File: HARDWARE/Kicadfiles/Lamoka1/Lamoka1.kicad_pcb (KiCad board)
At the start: 2 copper layers, 95 x 95 mm, 124 parts, among them IC1 INA240A2DR, J1 2606-1108/010-000, J2 2606-1352, J3 USB_C_Receptacle_USB2.0_14P, J4 470531000, J5 2604-1103, Q1 25V 60A N-Ch, Q2 30V 56A N-Ch, Q3 100V 150A N-Ch, Q4 100V 150A N-Ch, Q5 100V 150A N-Ch, Q6 100V 150A N-Ch, SW1 B3F-4055, U1 RP2354A, U10 ADS7128IRTER, U2 AMS1117-3.3, U3 74AHCT1G125, U4 LM5122MH/NOPB, U5 UCC27735DR, U6 UCC27735DR, U7 TPS62160DSGR, U8 TMP235A2DBZR, U9 TMP235A2DBZR, X1 ABM8-272-T3

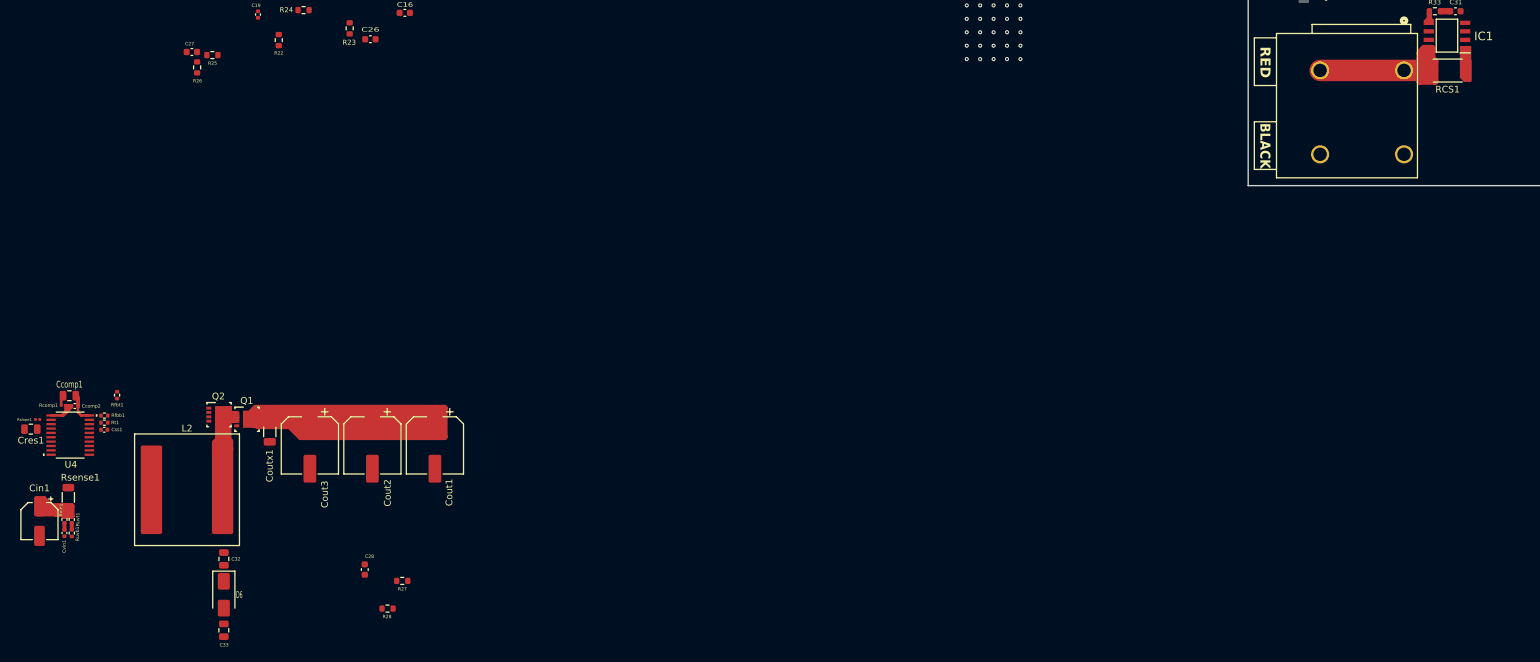
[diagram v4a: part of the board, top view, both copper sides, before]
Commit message: general routing for the Lamoka1/2
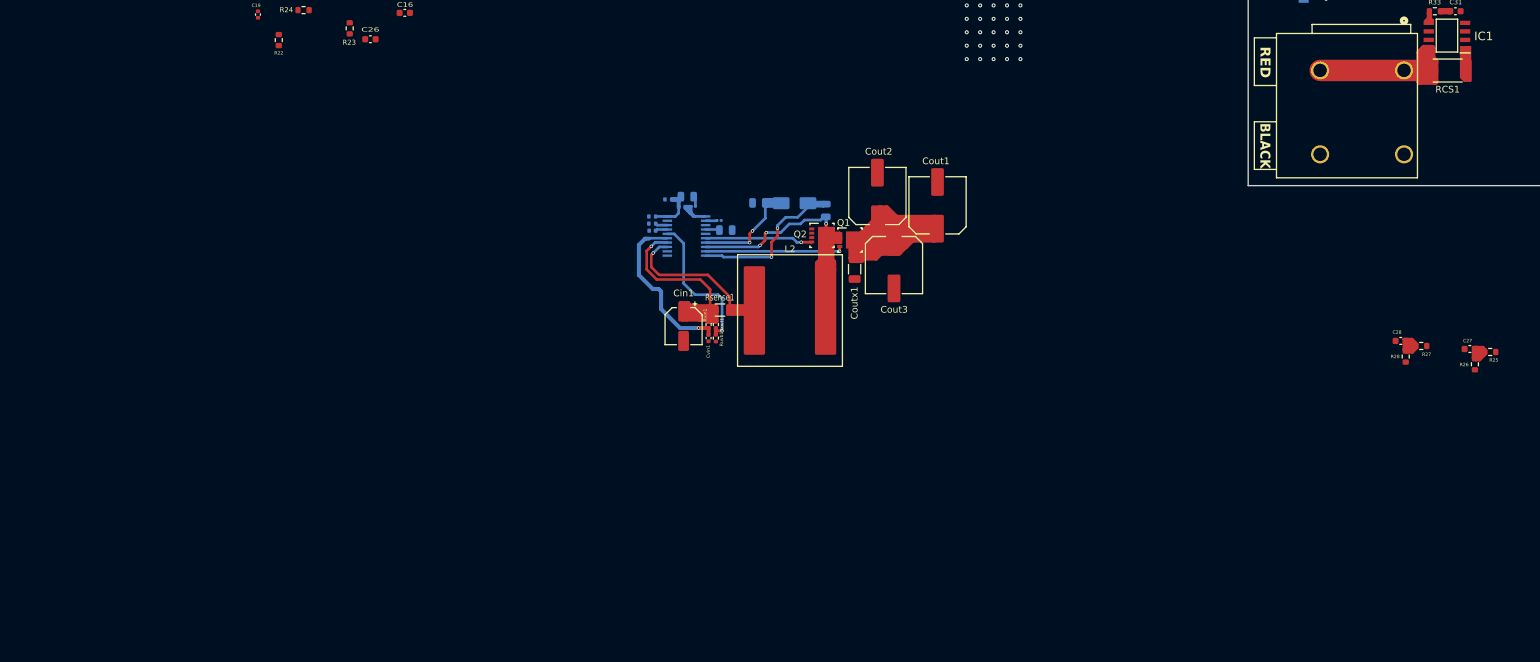
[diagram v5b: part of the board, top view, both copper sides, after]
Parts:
- C32, C33, Ccomp1, Ccomp2, Cres1, Css1, D6, Rcomp1, Rfbb1, Rfbt1, Rslope1, Rt1, U4: moved to B.Cu
- moved C27 195.4 mm to (365.1, 299.9)
- moved R25 195.4 mm to (368.2, 300.4)
- moved R26 195.4 mm to (365.9, 302.2)
- moved C28 158.0 mm to (354.9, 298.7), turned to 180 degrees
- moved R28 156.2 mm to (355.6, 301.1), turned to -90 degrees
- moved R27 155.8 mm to (357.9, 299.5)
- moved Cres1 107.7 mm to (254.3, 282.2), turned to 0 degrees
- moved Rslope1 105.8 mm to (253.3, 280.8), turned to 0 degrees
- moved C32 103.6 mm to (269.2, 279.3), turned to -90 degrees
- moved D6 103.1 mm to (264.6, 278.2), turned to 180 degrees
- moved C33 102.0 mm to (259.2, 278.2), turned to 0 degrees
- moved Rsense1 101.0 mm to (253.4, 294.1), turned to 0 degrees
- moved Cvin1 100.2 mm to (251.7, 298.3)
- moved Ruvb1 100.2 mm to (252.8, 298.3)
- moved Cin1 100.2 mm to (248.0, 296.5)
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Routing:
- net /Inversion-Section/G4D: track 238.8 -> 174.5 mm
- net /Inversion-Section/CSN: track 0.00 -> 54.0 mm, vias 0 -> 1
- net /Inversion-Section/BST: track 0.00 -> 35.6 mm, vias 0 -> 2
- net /Inversion-Section/CSP: track 157.9 -> 182.6 mm, vias 0 -> 1
- net /Inversion-Section/VCC: track 0.00 -> 24.5 mm, vias 0 -> 2
- net /Inversion-Section/VIN: track 1.02 -> 25.3 mm, vias 0 -> 1
- net /Inversion-Section/SW: track 56.8 -> 79.9 mm, vias 0 -> 3
- net /Inversion-Section/UVLO: track 1.00 -> 22.4 mm, vias 0 -> 1
- net /Inversion-Section/HO: track 0.00 -> 20.7 mm, vias 0 -> 1
- net /Control-Section/AIN0: track 0.00 -> 19.0 mm
- net /Control-Section/AIN1: track 0.00 -> 17.6 mm
- net /Inversion-Section/LO: track 0.00 -> 16.1 mm, vias 0 -> 1
- net /Inversion-Section/FB: track 4.48 -> 10.3 mm
- net /Inversion-Section/RES: track 0.00 -> 2.09 mm
- net /Inversion-Section/SYNCIN_RT: track 0.00 -> 1.83 mm
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
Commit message: more routing
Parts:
- removed H3, H4, H5, H6, H7, H8: MountingHole, MountingHole:MountingHole_3.2mm_M3
- C12, C13, U2: moved to F.Cu
- C16, C17, C18, C26, R22, R23, R24, R4, R7: moved to B.Cu
- moved H2 233.6 mm to (417.0, 270.4)
- moved C18 186.2 mm to (365.6, 225.4), turned to -100 degrees
- moved R24 183.2 mm to (374.4, 240.6), turned to 180 degrees
- moved C19 177.1 mm to (359.3, 221.1), turned to -90 degrees
- moved R23 176.4 mm to (374.4, 242.2), turned to 180 degrees
- moved R7 165.0 mm to (360.8, 216.2), turned to -90 degrees
- moved C26 163.2 mm to (364.1, 241.4), turned to 180 degrees
- moved C17 159.9 mm to (364.6, 225.2), turned to -100 degrees
- moved C15 159.4 mm to (360.5, 226.0), turned to 0 degrees
- moved C14 157.6 mm to (360.6, 222.2), turned to -90 degrees
- moved C16 156.8 mm to (361.2, 224.2), turned to 170 degrees
- moved R4 155.1 mm to (363.3, 225.4), turned to -100 degrees
- moved R22 154.9 mm to (341.3, 234.2), turned to 90 degrees
- moved Cout1 136.6 mm to (421.2, 259.9), turned to -90 degrees
- moved Cout2 136.4 mm to (412.2, 259.9), turned to -90 degrees
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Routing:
- net /Inversion-Section/CSP: track 182.6 -> 328.0 mm, vias 1 -> 2
- net /Buck-5v: track 49.9 -> 70.6 mm
- net /Control-Section/USB-5v: track 7.22 -> 23.3 mm
- net /Inversion-Section/G4D: track 174.5 -> 190.2 mm
- net /Control-Section/1V1: track 0.00 -> 12.9 mm, vias 0 -> 1
- net /Control-Section/BTN: track 0.00 -> 12.5 mm
- net /Control-Section/VREG_GND: track 0.00 -> 12.1 mm, vias 0 -> 1
- net /Inversion-Section/VIN: track 25.3 -> 19.4 mm
- net /Control-Section/3v3: track 0.00 -> 5.83 mm, vias 0 -> 1
- net Net-(U1-VREG_LX): track 0.00 -> 5.79 mm
- net /GPIO5: track 0.03 -> 4.71 mm
- net Net-(U1-VREG_AVDD): track 0.00 -> 4.53 mm
- net /Inversion-Section/CSN: track 54.0 -> 54.6 mm

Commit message: MORE ROUTING FOR THE LAMOKA1/2, JUST CONTROL RELATED STUFF HERE
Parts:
- U8: moved to B.Cu
- moved G*** 106.1 mm to (379.3, 218.7)
- moved NT1 67.3 mm to (360.9, 227.8), turned to -135 degrees
- moved C12 55.3 mm to (342.2, 211.9)
- moved C13 55.3 mm to (339.9, 207.2)
- moved U2 55.3 mm to (345.3, 207.2)
- moved U8 44.1 mm to (369.9, 227.5), turned to 0 degrees
- moved C26 29.7 mm to (380.5, 216.7)
- moved R23 29.7 mm to (390.7, 217.5)
- moved R24 29.7 mm to (390.7, 215.9)
- moved U10 29.7 mm to (384.2, 217.8)
- moved U9 22.7 mm to (409.7, 209.2)
- moved R5 3.94 mm to (350.1, 219.1)
- moved R6 3.94 mm to (350.1, 217.6)
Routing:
- net /Control-Section/AIN1: track 17.6 -> 91.6 mm, vias 0 -> 3
- net /Control-Section/AIN0: track 19.0 -> 92.3 mm, vias 0 -> 1
- net /Control-Section/AIN2: track 21.6 -> 74.2 mm, vias 0 -> 3
- net /GPIO5: track 4.71 -> 56.8 mm
- net /GPIO6: track 0.00 -> 49.5 mm
- net /Control-Section/AIN4: track 12.0 -> 56.7 mm, vias 0 -> 1
- net /Control-Section/GPIO8: track 0.00 -> 32.0 mm, vias 0 -> 2
- net /Control-Section/AIN3: track 19.3 -> 48.5 mm, vias 0 -> 3
- net /Control-Section/GPIO9: track 0.00 -> 26.8 mm
- net /Control-Section/5V: track 0.00 -> 12.6 mm
- net /Control-Section/D+: track 2.99 -> 15.5 mm
- net /Control-Section/USB_DP: track 0.00 -> 12.3 mm
- net /Control-Section/USB_DM: track 0.00 -> 11.8 mm
- net /Control-Section/D-: track 2.99 -> 13.3 mm
- net /Control-Section/XIN: track 0.00 -> 7.93 mm
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- added copper zone on B.Cu, net GND
- added copper zone on F.Cu, net GND
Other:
- board text removed: "Rated for 100% internal magic smoke retention."

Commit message: MOSFET ROUTING, AND SUCH
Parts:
- removed R22: 10k, Resistor_SMD:R_0603_1608Metric
- added J6: FAN 5V, Connector_Wire:SolderWirePad_1x01_SMD_3x6mm, B.Cu at (166.4, 158.6)
- C12, C13, U2: moved to B.Cu
- J4: value 470531000 -> FAN GND; footprint Connector:FanPinHeader_1x04_P2.54mm_Vertical -> Connector_Wire:SolderWirePad_1x01_SMD_3x6mm
- moved J4 190.0 mm to (166.4, 154.0), turned to -90 degrees
- moved G*** 188.0 mm to (209.0, 138.9)
- moved C1 188.0 mm to (194.4, 156.8)
- moved C11 188.0 mm to (185.5, 161.5)
- moved C15 188.0 mm to (190.2, 146.2)
- moved C16 188.0 mm to (190.9, 144.5)
- moved C2 188.0 mm to (201.7, 156.8)
- moved C20 188.0 mm to (202.9, 142.6)
- moved C22 188.0 mm to (232.4, 166.7)
- moved C25 188.0 mm to (168.5, 166.5)
- moved C31 188.0 mm to (192.7, 169.9)
- moved C33 188.0 mm to (212.8, 170.9)
- moved CR1 188.0 mm to (171.9, 146.9)
- moved Cout3 188.0 mm to (232.9, 180.2)
- moved Cvin1 188.0 mm to (205.3, 191.0)
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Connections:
- C25 pad 2: /Buck-5v -> /Control-Section/Buck-5v
- CR2 pad 2: /Buck-5v -> /Control-Section/Buck-5v
- L3 pad 1: /Buck-5v -> /Control-Section/Buck-5v
- R20 pad 1: /Buck-5v -> /Control-Section/Buck-5v
- R21 pad 1: /Buck-5v -> /Control-Section/Buck-5v
- U1 pad 8: /GPIO5 -> unconnected-(U1-GPIO5-Pad8)
- U1 pad 9: /GPIO6 -> unconnected-(U1-GPIO6-Pad9)
- U7 pad 6: /Buck-5v -> /Control-Section/Buck-5v
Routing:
- net /Inversion-Section/G4D: track 190.2 -> 446.9 mm, vias 0 -> 9
- net /BLUE: track 32.6 -> 203.0 mm, vias 0 -> 7
- net /BROWN: track 32.0 -> 170.2 mm, vias 0 -> 6
- net /Control-Section/Buck-5v: track 0.00 -> 110.5 mm
- net /Control-Section/5V: track 12.6 -> 109.7 mm
- net /Buck-5v: track 70.6 -> 0.00 mm
- net /GPIO5: track 56.8 -> 0.00 mm
- net /Control-Section/GPIO11: track 0.00 -> 53.8 mm, vias 0 -> 1
- net /Control-Section/3v3: track 13.7 -> 65.2 mm, vias 1 -> 2
- net /GPIO6: track 49.5 -> 0.00 mm
- net /Control-Section/BTN: track 12.5 -> 23.3 mm
- net GND: track 8.20 -> 0.00 mm, vias 25 -> 30
- net /Control-Section/AIN4: track 56.7 -> 62.0 mm
- net Net-(D1-DIN): track 1.99 -> 6.28 mm
- net /Control-Section/AIN3: track 48.5 -> 45.9 mm
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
